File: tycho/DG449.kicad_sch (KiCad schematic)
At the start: 1 part, among them U14 DG449

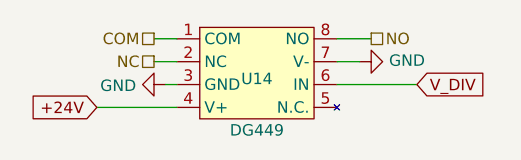
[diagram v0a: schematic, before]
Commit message: Remove global labels and replace with hierarchical and standard labels
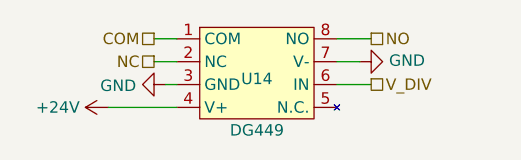
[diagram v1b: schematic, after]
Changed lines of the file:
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@@
     (stroke (width 0) (type default))
   )
-  (wire (pts (xy 162.56 109.22) (xy 171.45 109.22))
+  (wire (pts (xy 162.56 109.22) (xy 166.37 109.22))
     (stroke (width 0) (type default))
   )
@@
     (stroke (width 0) (type default))
   )
-  (wire (pts (xy 135.89 111.76) (xy 144.78 111.76))
+  (wire (pts (xy 137.16 111.76) (xy 144.78 111.76))
     (stroke (width 0) (type default))
   )
@@
     (stroke (width 0) (type default))
   )
-  (global_label "V_DIV" (shape input) (at 171.45 109.22 0) (fields_autoplaced)
+  (hierarchical_label "NO" (shape passive) (at 166.37 104.14 0) (fields_autoplaced)
     (effects (font (size 1.27 1.27)) (justify left))
-    (property "Intersheetrefs" "${INTERSHEET_REFS}" (at 179.4548 109.22 0)
-      (effects (font (size 1.27 1.27)) (justify left) hide)
-    )
   )
-  (global_label "+24V" (shape input) (at 135.89 111.76 180) (fields_autoplaced)
-    (effects (font (size 1.27 1.27)) (justify right))
-    (property "Intersheetrefs" "${INTERSHEET_REFS}" (at 127.8248 111.76 0)
-      (effects (font (size 1.27 1.27)) (justify right) hide)
-    )
-  )
-  (hierarchical_label "NO" (shape passive) (at 166.37 104.14 0) (fields_autoplaced)
+  (hierarchical_label "V_DIV" (shape passive) (at 166.37 109.22 0) (fields_autoplaced)
     (effects (font (size 1.27 1.27)) (justify left))
   )
@@
     (effects (font (size 1.27 1.27)) (justify right))
   )
+  (symbol (lib_id "power:+24V") (at 137.16 111.76 90) (unit 1)
+    (in_bom yes) (on_board yes) (dnp no) (fields_autoplaced)
+    (property "Reference" "#PWR070" (at 140.97 111.76 0)
+      (effects (font (size 1.27 1.27)) hide)
+    )
+    (property "Value" "+24V" (at 133.985 111.76 90)
+      (effects (font (size 1.27 1.27)) (justify left))
+    )
+    (property "Footprint" "" (at 137.16 111.76 0)
+      (effects (font (size 1.27 1.27)) hide)
+    )
+    (property "Datasheet" "" (at 137.16 111.76 0)
+      (effects (font (size 1.27 1.27)) hide)
+    )
+    (pin "1")
+    (instances
+      (project "tycho"
+        (path "/4ed1cbaf-15e8-40e5-8366-86487d525fd5"
+          (reference "#PWR070") (unit 1)
+        )
+        (path "/4ed1cbaf-15e8-40e5-8366-86487d525fd5/6d08e03c-4f34-4618-a021-d4fe7d47286c"
+          (reference "#PWR089") (unit 1)
+        )
+        (path "/4ed1cbaf-15e8-40e5-8366-86487d525fd5/845eae9c-e6cd-483e-8ea7-d8fa122a86af"
+          (reference "#PWR096") (unit 1)
+        )
+      )
+    )
+  )
   (symbol (lib_id "power:GND") (at 165.1 106.68 90) (unit 1)

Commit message: Update revision number, metadata, and schematic page numbers
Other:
- company: (none) -> Copyright 2023 Great Scott Gadgets
- title: (none) -> Tycho
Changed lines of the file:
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@@
 (kicad_sch (version 20230121) (generator eeschema)
   (paper "A4")
+  (title_block
+    (title "Tycho")
+    (date "${DATE}")
+    (rev "${VERSION}")
+    (company "Copyright 2023 Great Scott Gadgets")
+    (comment 1 "Licensed under the CERN-OHL-P v2")
+  )
   (wire (pts (xy 143.51 109.22) (xy 144.78 109.22))
     (stroke (width 0) (type default))
